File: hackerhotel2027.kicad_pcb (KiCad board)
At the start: 4 copper layers, 95.4 x 99.9 mm, 346 parts, among them J1 USB device, U1 CH643Q, U2 TPD4E05U06DQAR

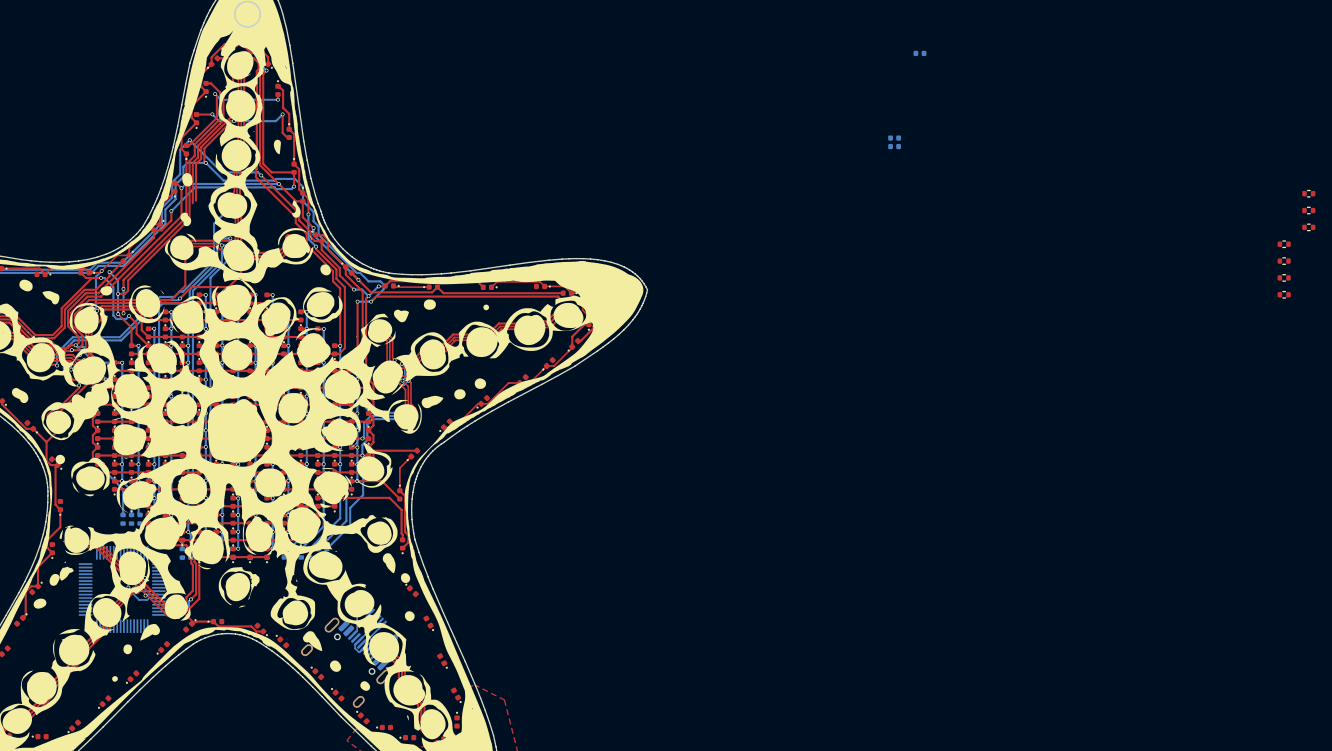
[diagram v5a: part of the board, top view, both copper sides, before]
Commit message: Add battery circuit, more routing
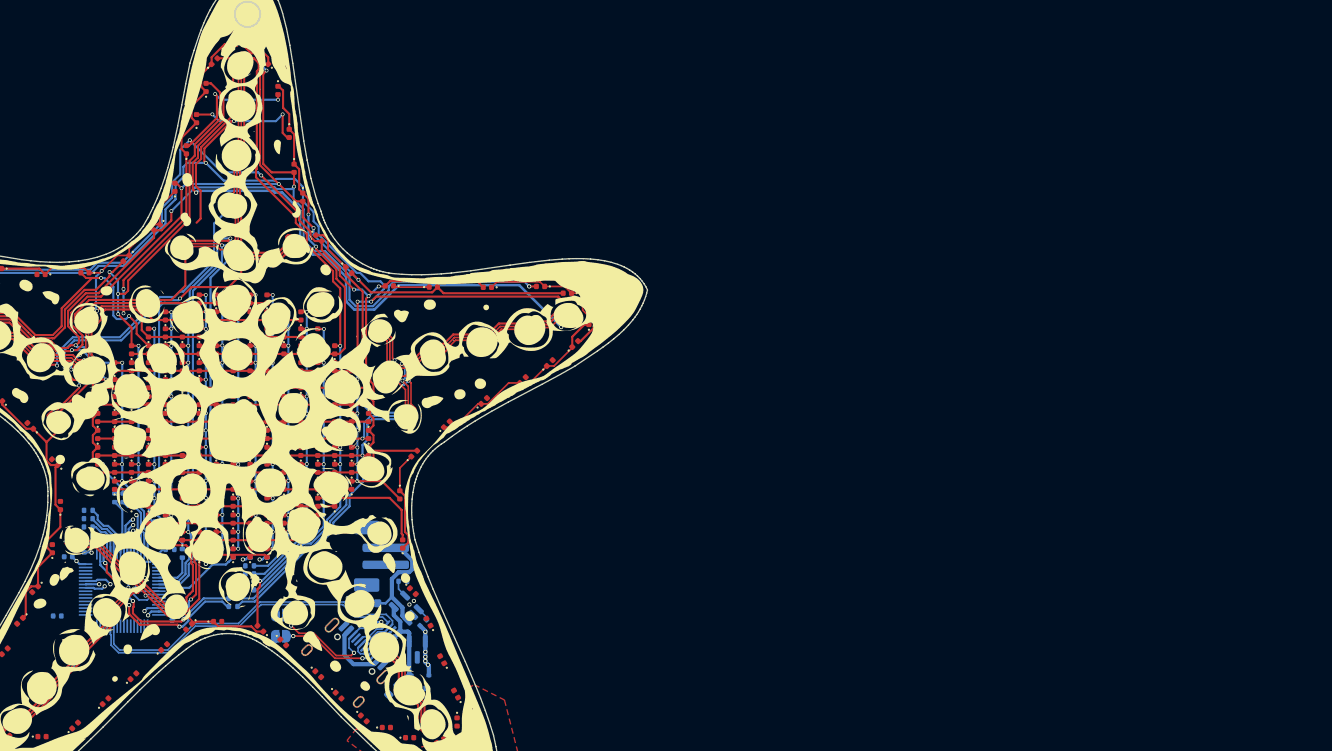
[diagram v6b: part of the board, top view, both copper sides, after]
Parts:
- added C54: 10uF, Capacitor_SMD:C_0603_1608Metric, B.Cu at (18.1, 30.3)
- added C55: 100nF, Capacitor_SMD:C_0402_1005Metric, B.Cu at (19.4, 30.7)
- added C56: 10uF, Capacitor_SMD:C_0603_1608Metric, B.Cu at (15.5, 20.0)
- added D316: 1N5819WS, Diode_SMD:D_SOD-323, B.Cu at (21.3, 28.6)
- added J2: Battery, Connector_JST:JST_PH_B2B-PH-SM4-TB_1x02-1MP_P2.00mm_Vertical, B.Cu at (16.7, 14.5)
- added JP1: CC2, Jumper:SolderJumper-2_P1.3mm_Open_RoundedPad1.0x1.5mm, B.Cu at (4.83, 21.4)
- added JP2: CC1, Jumper:SolderJumper-2_P1.3mm_Open_RoundedPad1.0x1.5mm, B.Cu at (4.83, 23.9)
- added Q1: JSM2301S, Package_TO_SOT_SMD:SOT-23, B.Cu at (20.9, 25.5)
- added R27: 2k, Resistor_SMD:R_0402_1005Metric, B.Cu at (19.2, 17.4)
- added R28: 10k, Resistor_SMD:R_0402_1005Metric, B.Cu at (21.6, 22.3)
- added R29: 100k, Resistor_SMD:R_0402_1005Metric, B.Cu at (21.4, 30.1)
- added U4: XT4054K421MR-G, Package_TO_SOT_SMD:SOT-23-5, B.Cu at (19.6, 20.6)
- R18, R19, R20, R21, R22, R23, R24: moved to B.Cu
- moved R24 149.5 mm to (-18.4, 13.5), turned to 90 degrees
- moved R22 145.5 mm to (-14.8, 7.57), turned to 90 degrees
- moved R18 145.4 mm to (-17.9, 12.0), turned to 180 degrees
- moved R19 144.7 mm to (-17.9, 11.0), turned to 180 degrees
- moved R20 144.1 mm to (-17.9, 10.0), turned to 180 degrees
- moved R21 143.5 mm to (-17.9, 9.05), turned to 180 degrees
- moved R23 140.4 mm to (-8.26, 13.7)
- moved C2 116.9 mm to (-20.3, 14.5)
- moved C1 113.4 mm to (-21.6, 21.5)
- moved C3 102.3 mm to (-8.01, 21.6), turned to -90 degrees
- moved R17 12.7 mm to (-0.80, 20.4), turned to 0 degrees
- moved R16 11.4 mm to (-0.80, 19.4), turned to 0 degrees
- moved R15 8.33 mm to (1.15, 18.4), turned to 0 degrees
- moved R14 6.98 mm to (1.15, 17.5), turned to 0 degrees
- moved R13 5.66 mm to (1.15, 16.6), turned to 0 degrees
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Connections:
- C1 pad 1: +3.3V -> VCC
- C2 pad 1: +3.3V -> VCC
- C3 pad 1: +3.3V -> VCC
- J1 pad A5: CC1 -> /CC1
- J1 pad B5: CC2 -> /CC2
- R25 pad 2: CC1 -> /CC1
- R26 pad 2: CC2 -> /CC2
- U1 pad 31: unconnected-(U1-VDD31-Pad31) -> VCC
- U1 pad 52: unconnected-(U1-PB22-Pad52) -> CHRG
- U1 pad 55: CC1 -> CC1_ALT
- U1 pad 56: CC2 -> CC2_ALT
- U1 pad 64: unconnected-(U1-VDD-Pad64) -> VCC
- U2 pad 1: USB_DN -> USB_DP
- U2 pad 10: USB_DN -> USB_DP
- U2 pad 2: USB_DP -> USB_DN
- U2 pad 9: USB_DP -> USB_DN
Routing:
- net Net-(D308-A): track 17.9 -> 73.6 mm, vias 0 -> 2
- net USB_DN: track 5.44 -> 46.1 mm
- net /R2b: track 121.3 -> 159.7 mm, vias 13 -> 14
- net USB_DP: track 6.33 -> 43.0 mm
- net VBUS: track 1.64 -> 26.2 mm
- net R11: track 0.00 -> 23.5 mm, vias 0 -> 2
- net R17: track 0.00 -> 22.5 mm, vias 0 -> 4
- net R16: track 0.00 -> 21.7 mm, vias 0 -> 2
- net R9: track 0.00 -> 21.5 mm, vias 0 -> 2
- net R10: track 0.00 -> 16.8 mm, vias 0 -> 2
- net Net-(J2-Pin_1): track 0.00 -> 15.3 mm
- net /CC2: track 0.00 -> 15.1 mm, vias 0 -> 2
- net R24: track 0.00 -> 13.9 mm, vias 0 -> 2
- net /CC1: track 0.00 -> 13.5 mm, vias 0 -> 2
- net Net-(D116-A): track 165.8 -> 178.3 mm
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- added copper zone on In1.Cu, net VCC
